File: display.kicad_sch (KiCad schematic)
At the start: 303 parts, among them U4 74HC595, U5 74HC595, U6 74HC595

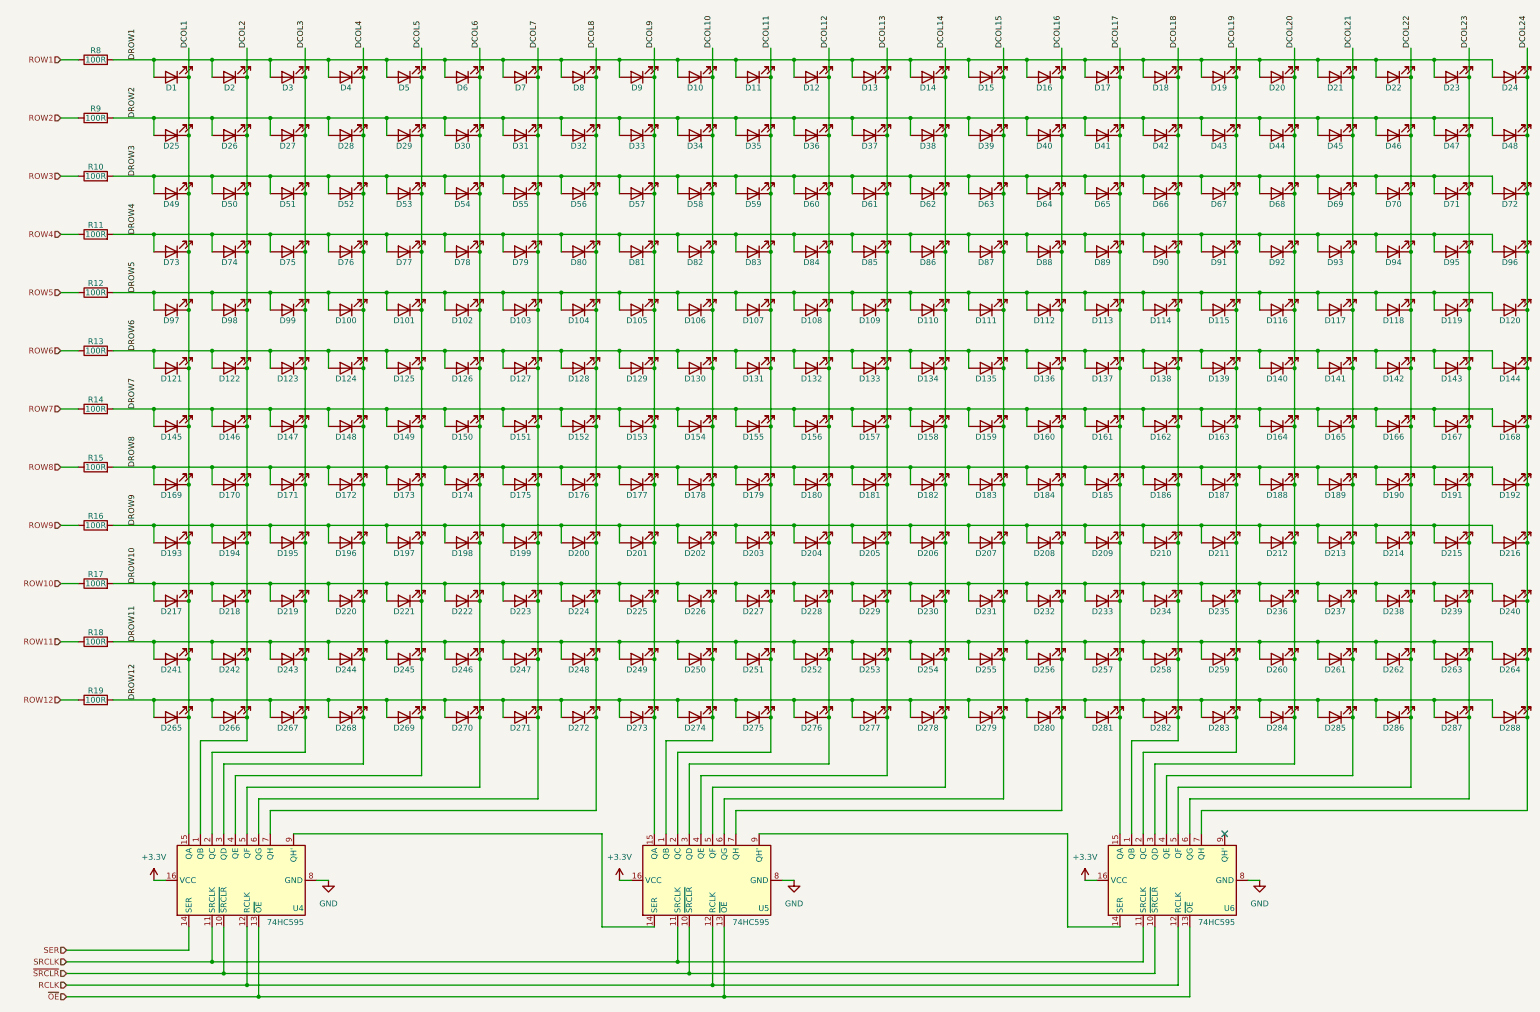
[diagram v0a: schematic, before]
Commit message: Updated badge based on feedback from badge.team
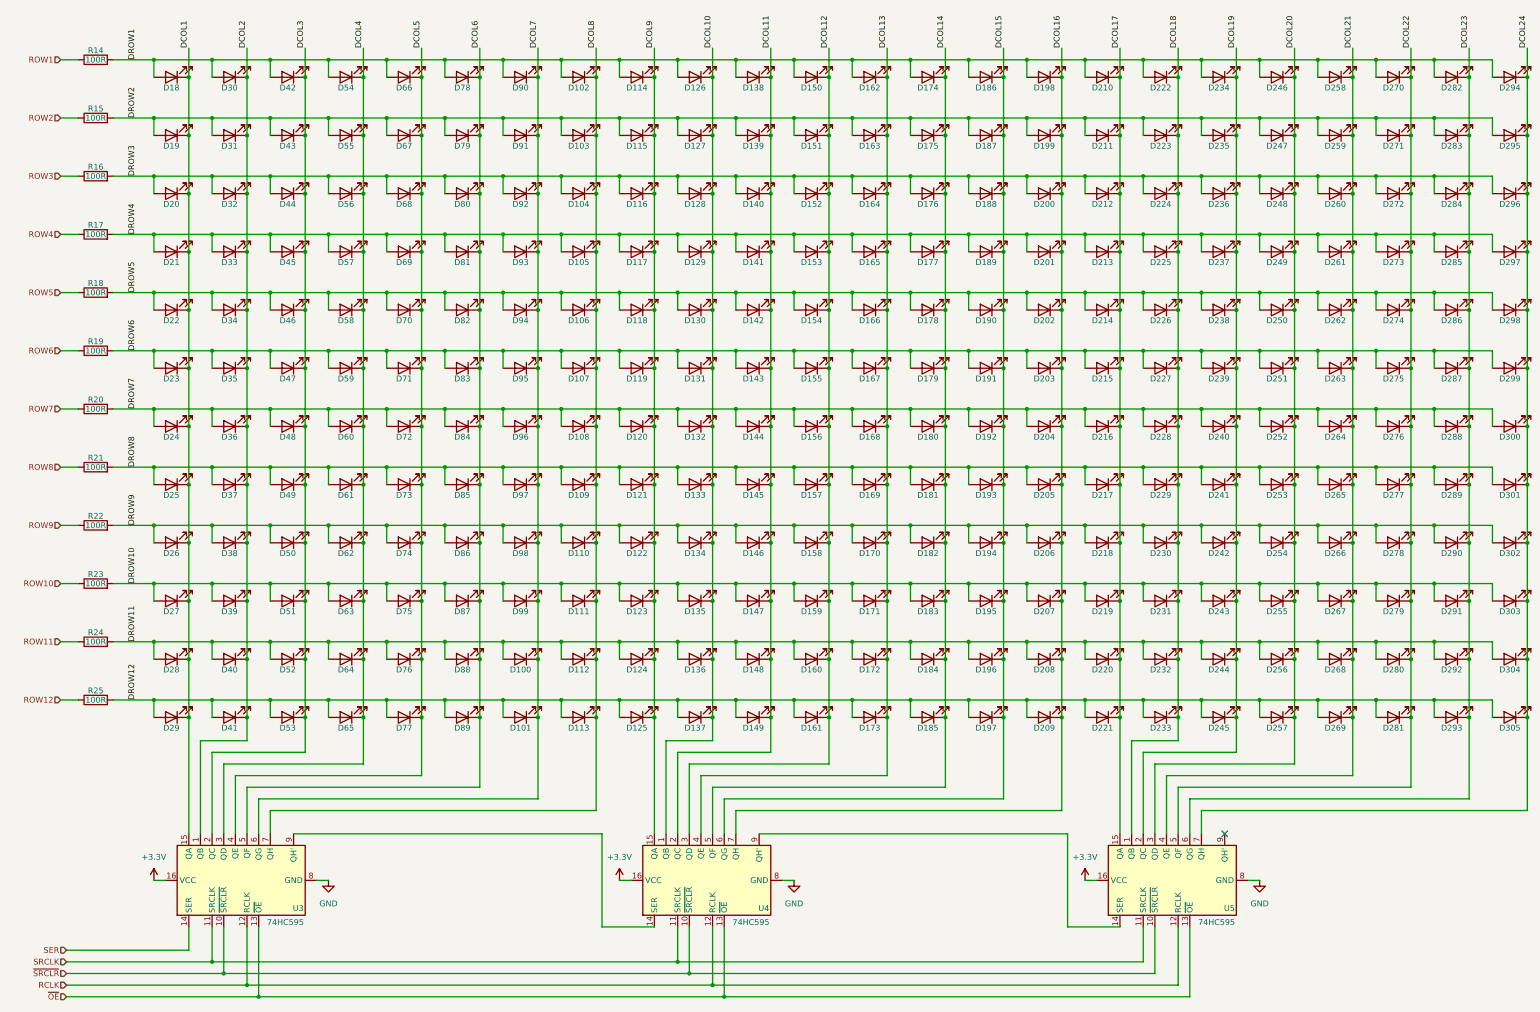
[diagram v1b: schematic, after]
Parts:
- renumbered D247 to D100, D271 to D101, D8 to D102, D32 to D103, D56 to D104, D80 to D105, D104 to D106, D128 to D107, D152 to D108, D176 to D109, D200 to D110, D224 to D111, D248 to D112, D272 to D113, D9 to D114, D33 to D115, D57 to D116, D81 to D117, D105 to D118, D129 to D119, D153 to D120, D177 to D121, D201 to D122, D225 to D123, D249 to D124, D273 to D125, D10 to D126, D34 to D127, D58 to D128, D82 to D129, D106 to D130, D130 to D131, D154 to D132, D178 to D133, D202 to D134, D226 to D135, D250 to D136, D274 to D137, D11 to D138, D35 to D139, D59 to D140, D83 to D141, D107 to D142, D131 to D143, D155 to D144, D179 to D145, D203 to D146, D227 to D147, D251 to D148, D275 to D149, D12 to D150, D36 to D151, D60 to D152, D84 to D153, D108 to D154, D132 to D155, D180 to D157, D204 to D158, D228 to D159, D252 to D160, D276 to D161, D13 to D162, D37 to D163, D61 to D164, D85 to D165, D109 to D166, D133 to D167, D157 to D168, D181 to D169, D205 to D170, D229 to D171, D253 to D172, D277 to D173, D14 to D174, D38 to D175, D62 to D176, D86 to D177, D110 to D178, D134 to D179, D1 to D18, D158 to D180, D182 to D181, D206 to D182, D230 to D183, D254 to D184, D278 to D185, D15 to D186, D39 to D187, D63 to D188, D87 to D189, D25 to D19, D111 to D190, D135 to D191, D159 to D192, D183 to D193, D207 to D194, D231 to D195, D255 to D196, D279 to D197, D16 to D198, D40 to D199, D49 to D20, D64 to D200, D88 to D201, D112 to D202, D136 to D203, D160 to D204, D184 to D205, D208 to D206, D232 to D207, D256 to D208, D280 to D209, D73 to D21, D17 to D210, D41 to D211, D65 to D212, D89 to D213, D113 to D214, D137 to D215, D161 to D216, D185 to D217, D209 to D218, D233 to D219, D97 to D22, D257 to D220, D281 to D221, D18 to D222, D42 to D223, D66 to D224, D90 to D225, D114 to D226, D138 to D227, D162 to D228, D186 to D229, D121 to D23, D210 to D230, D234 to D231, D258 to D232, D282 to D233, D19 to D234, D43 to D235, D67 to D236, D91 to D237, D115 to D238, D139 to D239, D145 to D24, D163 to D240, D187 to D241, D211 to D242, D235 to D243, D259 to D244, D283 to D245, D20 to D246, D44 to D247, D68 to D248, D92 to D249, D169 to D25, D116 to D250, D140 to D251, D164 to D252, D188 to D253, D212 to D254, D236 to D255, D260 to D256, D284 to D257, D21 to D258, D45 to D259, D193 to D26, D69 to D260, D93 to D261, D117 to D262, D141 to D263, D165 to D264, D189 to D265, D213 to D266, D237 to D267, D261 to D268, D285 to D269, D217 to D27, D22 to D270, D46 to D271, D70 to D272, D94 to D273, D118 to D274, D142 to D275, D166 to D276, D190 to D277, D214 to D278, D238 to D279, D241 to D28, D262 to D280, D286 to D281, D23 to D282, D47 to D283, D71 to D284, D95 to D285, D119 to D286, D143 to D287, D167 to D288, D191 to D289, D265 to D29, D215 to D290, D239 to D291, D263 to D292, D287 to D293, D24 to D294, D48 to D295, D72 to D296, D96 to D297, D120 to D298, D144 to D299, D2 to D30, D168 to D300, D192 to D301, D216 to D302, D240 to D303, D264 to D304, D288 to D305, D26 to D31, D50 to D32, D74 to D33, D98 to D34, D122 to D35, D146 to D36, D170 to D37, D194 to D38, D218 to D39, D242 to D40, D266 to D41, D3 to D42, D27 to D43, D51 to D44, D75 to D45, D99 to D46, D123 to D47, D147 to D48, D171 to D49, D195 to D50, D219 to D51, D243 to D52, D267 to D53, D4 to D54, D28 to D55, D52 to D56, D76 to D57, D100 to D58, D124 to D59, D148 to D60, D172 to D61, D196 to D62, D220 to D63, D244 to D64, D268 to D65, D5 to D66, D29 to D67, D53 to D68, D77 to D69, D101 to D70, D125 to D71, D149 to D72, D173 to D73, D197 to D74, D221 to D75, D245 to D76, D269 to D77, D6 to D78, D30 to D79, D54 to D80, D78 to D81, D102 to D82, D126 to D83, D150 to D84, D174 to D85, D198 to D86, D222 to D87, D246 to D88, D270 to D89, D7 to D90, D31 to D91, D55 to D92, D79 to D93, D103 to D94, D127 to D95, D151 to D96, D175 to D97, D199 to D98, D223 to D99, R8 to R14, R9 to R15, R10 to R16, R11 to R17, R12 to R18, R13 to R19, R14 to R20, R15 to R21, R16 to R22, R17 to R23, R18 to R24, R19 to R25, U4 to U3, U5 to U4, U6 to U5
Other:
- company: (none) -> Marian Buschsieweke
- title: (none) -> Badge for RIOT Summit '25
